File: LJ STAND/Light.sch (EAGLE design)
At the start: 182 parts

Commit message: Light PCB routing
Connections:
- removed net N$43: U$1.S7
- removed net N$44: U$1.S8
- removed net N$45: U$1.S9
- removed net N$46: U$1.S10
- removed net N$47: U$1.S11
- removed net N$48: U$1.S12
- removed net N$49: U$1.S13
- removed net N$50: U$1.S14
- removed net N$51: U$1.S15
- removed net N$52: U$1.S16
- removed net N$57: U$1.S32
- removed net N$58: U$1.S31
- removed net N$59: U$1.S30
- removed net N$60: U$1.S29
- removed net N$61: U$1.S28
- removed net N$62: U$1.S27
- removed net N$63: U$1.S26
- removed net N$64: U$1.S25
- removed net N$65: U$1.S24
- removed net N$66: U$1.S23
- removed net N$67: U$1.S22
- removed net N$68: U$1.S21
- removed net N$69: U$1.S20
- removed net N$70: U$1.S19
- removed net N$71: U$1.S18
- removed net N$72: U$1.S17
- net LS10: now also U$1.S7
- net LS11: now also U$1.S8
- net LS12: now also U$1.S9
- net LS13: now also U$1.S10
- net LS14: now also U$1.S11
- net LS15: now also U$1.S12
- net LS16: now also U$1.S13
- net LS17: now also U$1.S14
- net LS18: now also U$1.S15
- net LS19: now also U$1.S16
- net LS20: now also U$1.S17
- net LS21: now also U$1.S18
- net LS22: now also U$1.S19
- net LS23: now also U$1.S20
- net LS24: now also U$1.S21
- net LS25: now also U$1.S22
- net LS26: now also U$1.S23
- net LS27: now also U$1.S24
- net LS28: now also U$1.S25
- net LS29: now also U$1.S26
- net LS30: now also U$1.S27
- net LS31: now also U$1.S28
- net LS32: now also U$1.S29
- net LS33: now also U$1.S30
- net LS34: now also U$1.S31
- net LS35: now also U$1.S32

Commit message: Finished routing light & encoder pcbs
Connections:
- net 3.3V: now also JP1.9; no longer JP1.1
- net A0: now also JP1.4; no longer JP1.7
- net A1: now also JP1.2; no longer JP1.8
- net A2: now also JP1.6; no longer JP1.9
- net A3: now also JP1.8; no longer JP1.10
- net A4: now also JP1.10; no longer JP1.11
- net EN: now also JP1.16; no longer JP1.13
- net GND: now also JP1.11, JP1.13; no longer JP1.14, JP1.16
- net LS0: now also JP1.7; no longer JP1.2
- net LS1: now also JP1.5; no longer JP1.3
- net LS10: now also U$1.S15; no longer U$1.S7
- net LS11: now also U$1.S16; no longer U$1.S8
- net LS12: now also U$1.S32; no longer U$1.S9
- net LS13: now also U$1.S31; no longer U$1.S10
- net LS14: now also U$1.S30; no longer U$1.S11
- net LS15: now also U$1.S29; no longer U$1.S12
- net LS16: now also U$1.S28; no longer U$1.S13
- net LS17: now also U$1.S27; no longer U$1.S14
- net LS18: now also U$1.S26; no longer U$1.S15
- net LS19: now also U$1.S25; no longer U$1.S16
- net LS2: now also JP1.3; no longer JP1.4
- net LS20: now also U$1.S24; no longer U$1.S17
- net LS21: now also U$1.S23; no longer U$1.S18
- net LS22: now also U$1.S22; no longer U$1.S19
- net LS23: now also U$1.S21; no longer U$1.S20
- net LS24: now also U$1.S20; no longer U$1.S21
- net LS25: now also U$1.S19; no longer U$1.S22
- net LS26: now also U$1.S18; no longer U$1.S23
- net LS27: now also U$1.S17; no longer U$1.S24
- net LS28: now also U$1.S1; no longer U$1.S25
- net LS29: now also U$1.S2; no longer U$1.S26
- net LS3: now also JP1.1; no longer JP1.5
- net LS30: now also U$1.S3; no longer U$1.S27
- net LS31: now also U$1.S4; no longer U$1.S28
- net LS32: now also U$1.S5; no longer U$1.S29
- net LS33: now also U$1.S6; no longer U$1.S30
- net LS34: now also U$1.S7; no longer U$1.S31
- net LS35: now also U$1.S8; no longer U$1.S32
- net LS4: now also U$1.S12; no longer U$1.S1
- net LS5: now also U$1.S11; no longer U$1.S2
- net LS6: now also U$1.S10; no longer U$1.S3
- net LS7: now also U$1.S9; no longer U$1.S4
- net LS8: now also U$1.S13; no longer U$1.S5
- net LS9: now also U$1.S14; no longer U$1.S6
- net MUX_OUT: now also JP1.15; no longer JP1.6
- net WR: now also JP1.14; no longer JP1.15

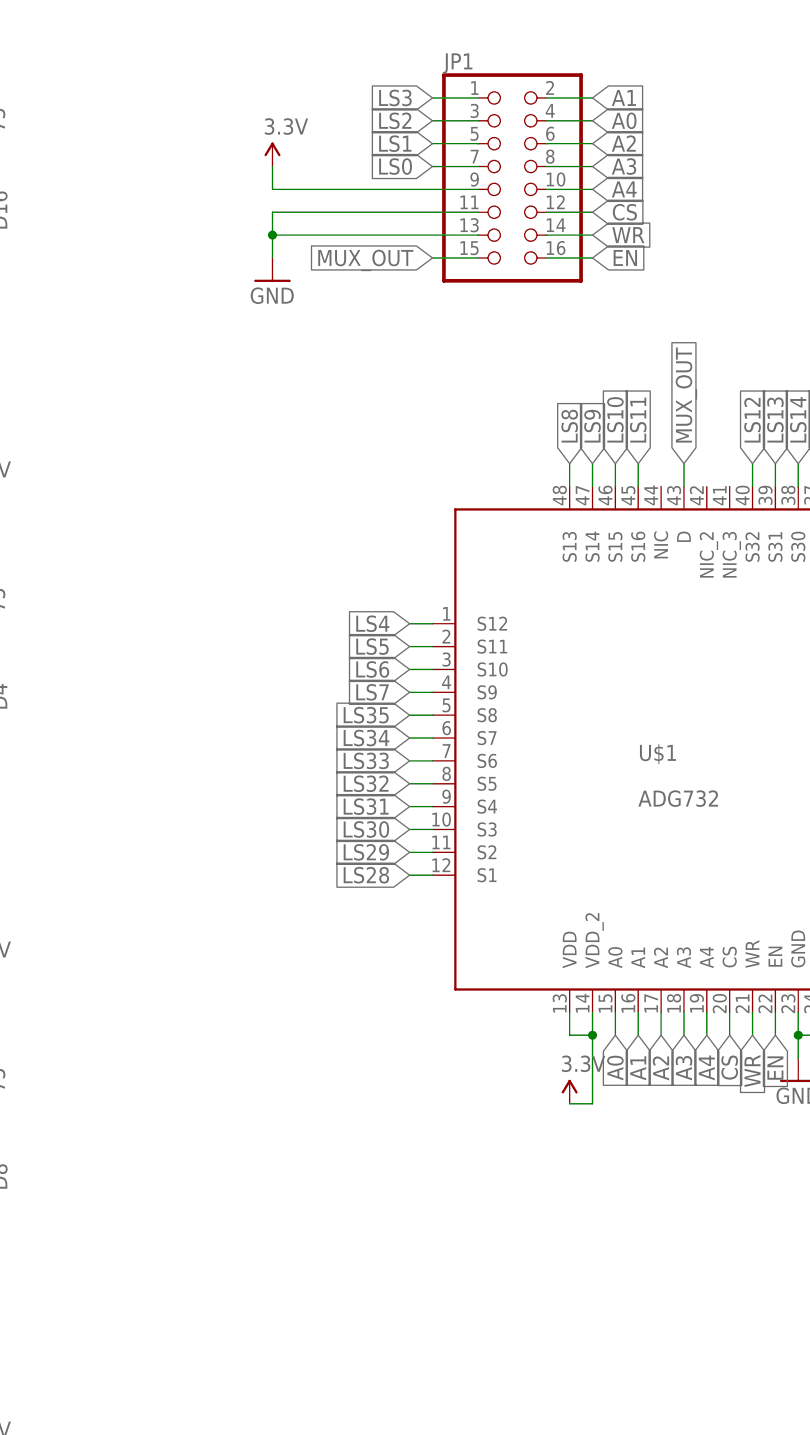
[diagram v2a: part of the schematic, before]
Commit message: Pin changes on teensys, removed some screen pins for motor grounding
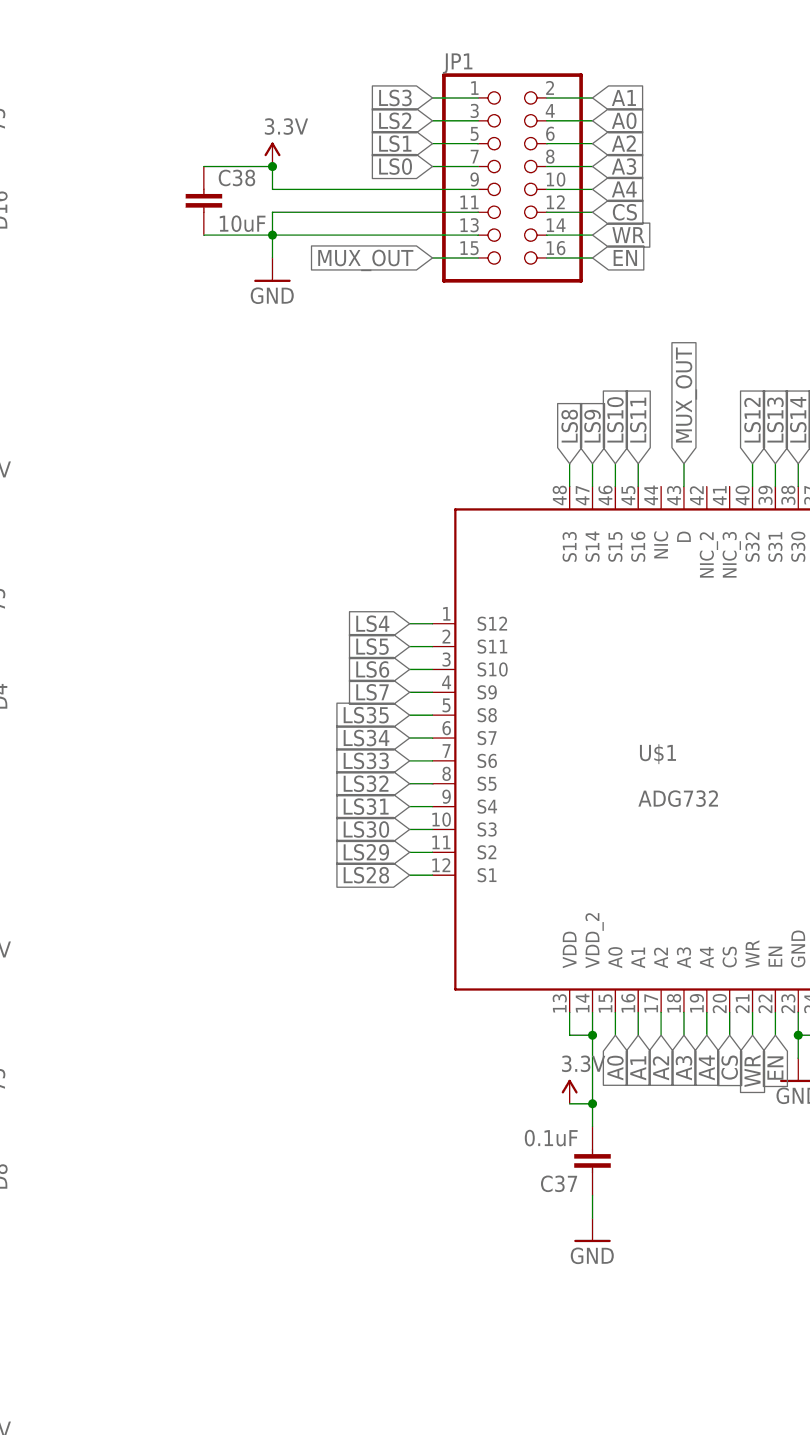
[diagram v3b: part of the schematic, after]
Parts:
- added C37: 0.1uF, SparkFun-Capacitors:CAP0603-CAP
- added C38: 10uF, SparkFun-Capacitors:CAP0805
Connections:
- net 3.3V: now also C37.2, C38.1
- net GND: now also C37.1, C38.2
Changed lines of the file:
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@@
 <?xml version="1.0" encoding="utf-8"?>
 <!DOCTYPE eagle SYSTEM "eagle.dtd">
-<eagle version="8.6.3">
+<eagle version="8.7.0">
 <drawing>
 <settings>
@@
 <part name="GND73" library="SparkFun-Aesthetics" deviceset="GND" device=""/>
 <part name="SUPPLY73" library="SparkFun-Aesthetics" deviceset="3.3V" device=""/>
+<part name="C37" library="SparkFun-Capacitors" deviceset="CAP" device="0603-CAP" value="0.1uF"/>
+<part name="GND75" library="SparkFun-Aesthetics" deviceset="GND" device=""/>
+<part name="C38" library="SparkFun-Capacitors" deviceset="CAP" device="0805" value="10uF"/>
 </parts>
 <sheets>
@@
 <instance part="GND73" gate="1" x="248.92" y="93.98"/>
 <instance part="SUPPLY73" gate="G$1" x="248.92" y="106.68"/>
+<instance part="C37" gate="G$1" x="284.48" y="-2.54" rot="R180"/>
+<instance part="GND75" gate="1" x="284.48" y="-12.7"/>
+<instance part="C38" gate="G$1" x="241.3" y="101.6"/>
 </instances>
 <busses>
@@
 <wire x1="248.92" y1="101.6" x2="248.92" y2="99.06" width="0.1524" layer="91"/>
 <junction x="248.92" y="99.06"/>
+<pinref part="C38" gate="G$1" pin="2"/>
+<wire x1="241.3" y1="99.06" x2="248.92" y2="99.06" width="0.1524" layer="91"/>
+</segment>
+<segment>
+<pinref part="C37" gate="G$1" pin="1"/>
+<pinref part="GND75" gate="1" pin="GND"/>
+<wire x1="284.48" y1="-10.16" x2="284.48" y2="-7.62" width="0.1524" layer="91"/>
 </segment>
 </net>
@@
 <wire x1="284.48" y1="2.54" x2="281.94" y2="2.54" width="0.1524" layer="91"/>
 <pinref part="SUPPLY74" gate="G$1" pin="3.3V"/>
+<pinref part="C37" gate="G$1" pin="2"/>
+<wire x1="284.48" y1="2.54" x2="284.48" y2="0" width="0.1524" layer="91"/>
+<junction x="284.48" y="2.54"/>
 </segment>
 <segment>
@@
 <pinref part="SUPPLY73" gate="G$1" pin="3.3V"/>
 <wire x1="248.92" y1="104.14" x2="248.92" y2="106.68" width="0.1524" layer="91"/>
+<pinref part="C38" gate="G$1" pin="1"/>
+<wire x1="248.92" y1="106.68" x2="241.3" y2="106.68" width="0.1524" layer="91"/>
+<junction x="248.92" y="106.68"/>
 </segment>
 </net>
